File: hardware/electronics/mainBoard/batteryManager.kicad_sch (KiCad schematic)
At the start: 33 parts, among them J20 S3B-XH-SM4-TB, J21 1726480102, Q3 BUK6D72-30EX, Q4 BUK6D72-30EX, U23 BQ76905

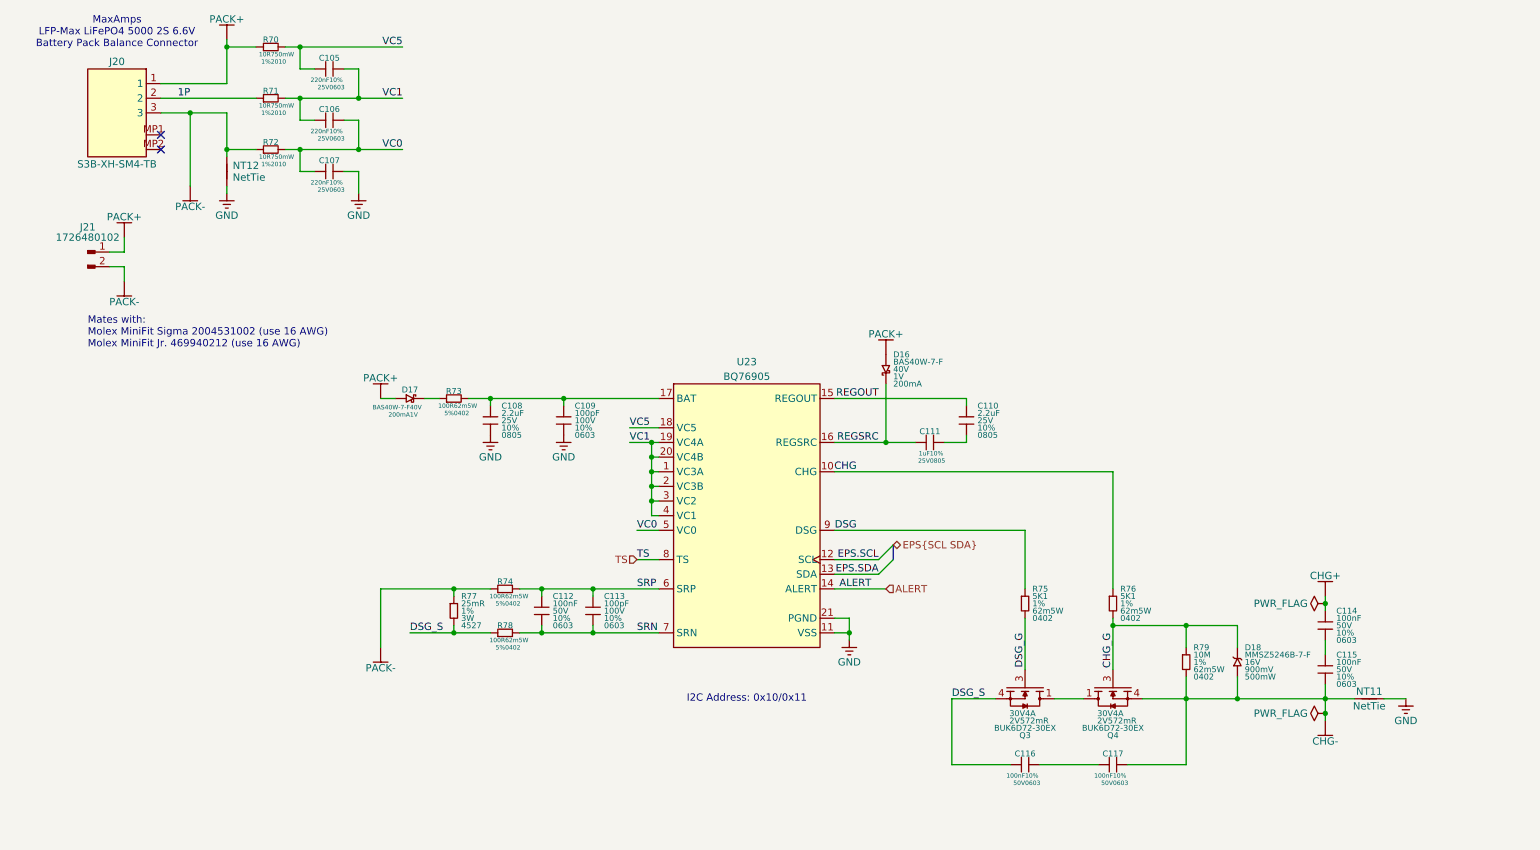
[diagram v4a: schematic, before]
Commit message: updated capacitors
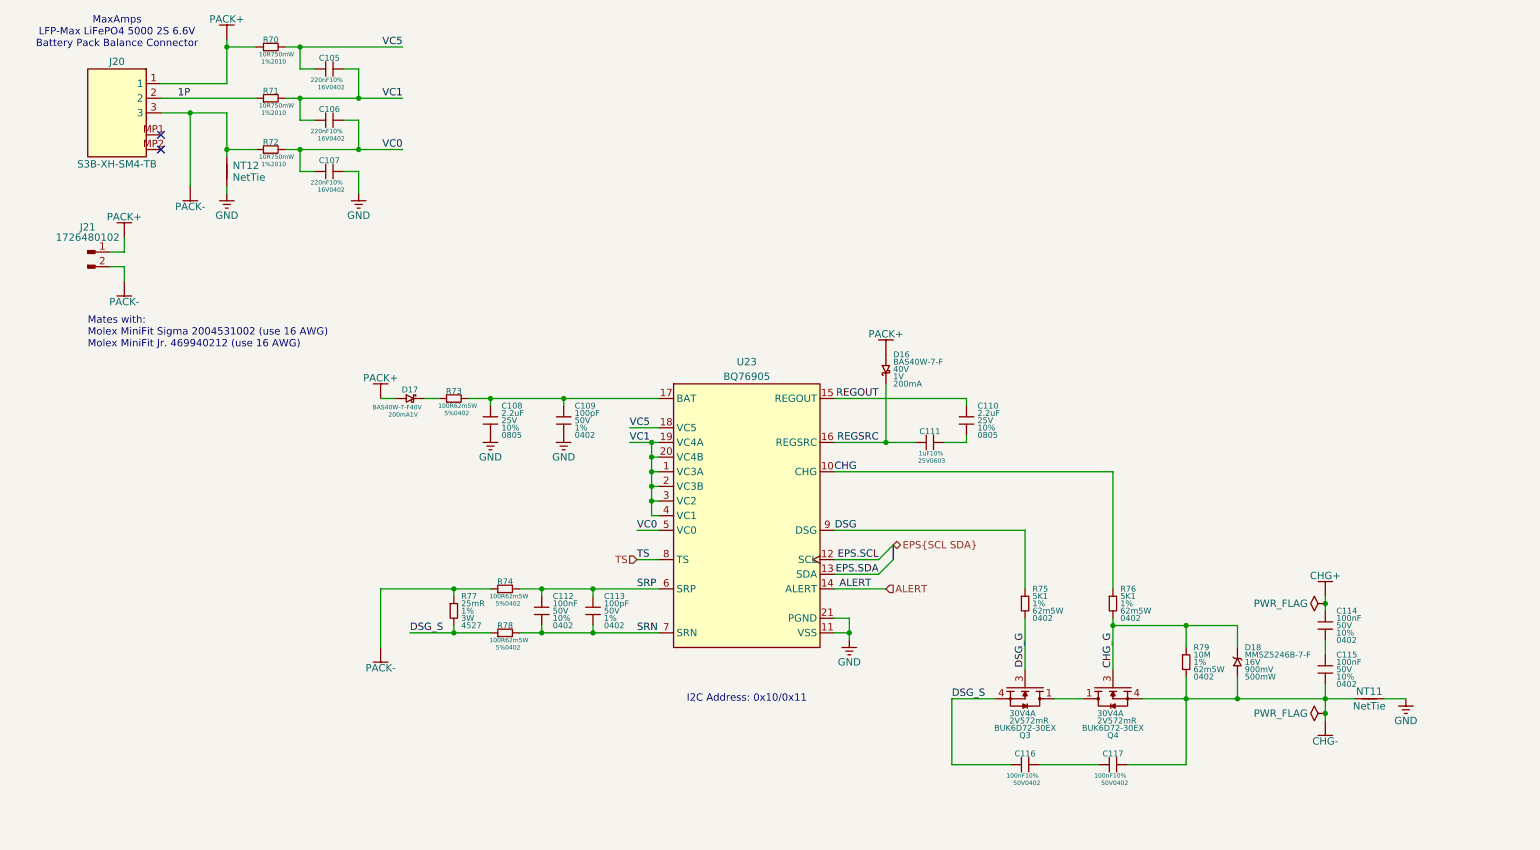
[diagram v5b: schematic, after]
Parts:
- C105, C106, C107: DKPN 478-KAM15BR71E224KTCT-ND -> 490-GRT155R71C224KE01DCT-ND; MPN KAM15BR71E224KT -> GRT155R71C224KE01D; Manufacturer KYOCERA AVX -> Murata Electronics; Package 0603 -> 0402; Voltage Rating 25V -> 16V
- C108, C110: DKPN 478-KAM21KR71E225KUCT-ND -> 490-GRT21BR71E225KE13LCT-ND; MPN 08053C225K4T2A -> GRT21BR71E225KE13L; Manufacturer KYOCERA AVX -> Murata Electronics
- C109, C113: DKPN 478-06031C101K4T2ACT-ND -> 490-14349-1-ND; MPN 06031C101K4T2A -> GCM1555C1H101FA16D; Manufacturer KYOCERA AVX -> Murata Electronics; Package 0603 -> 0402; Tolerance 10% -> 1%; Voltage Rating 100V -> 50V
- C111: DKPN 478-KAF21KR71E105KLCT-ND -> 490-GRT188R71E105KE13DCT-ND; MPN 08053C105K4Z4A -> GRT188R71E105KE13D; Manufacturer KYOCERA AVX -> Murata Electronics; Package 0805 -> 0603
- C112, C114, C115, C116, C117: DKPN 478-KAM15AR71H104KTCT-ND -> 490-GRT155R71H104KE01DCT-ND; MPN 06035C104K4T2A -> GRT155R71H104KE01D; Manufacturer KYOCERA AVX -> Murata Electronics; Package 0603 -> 0402

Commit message: added testpoints and fixed AGND
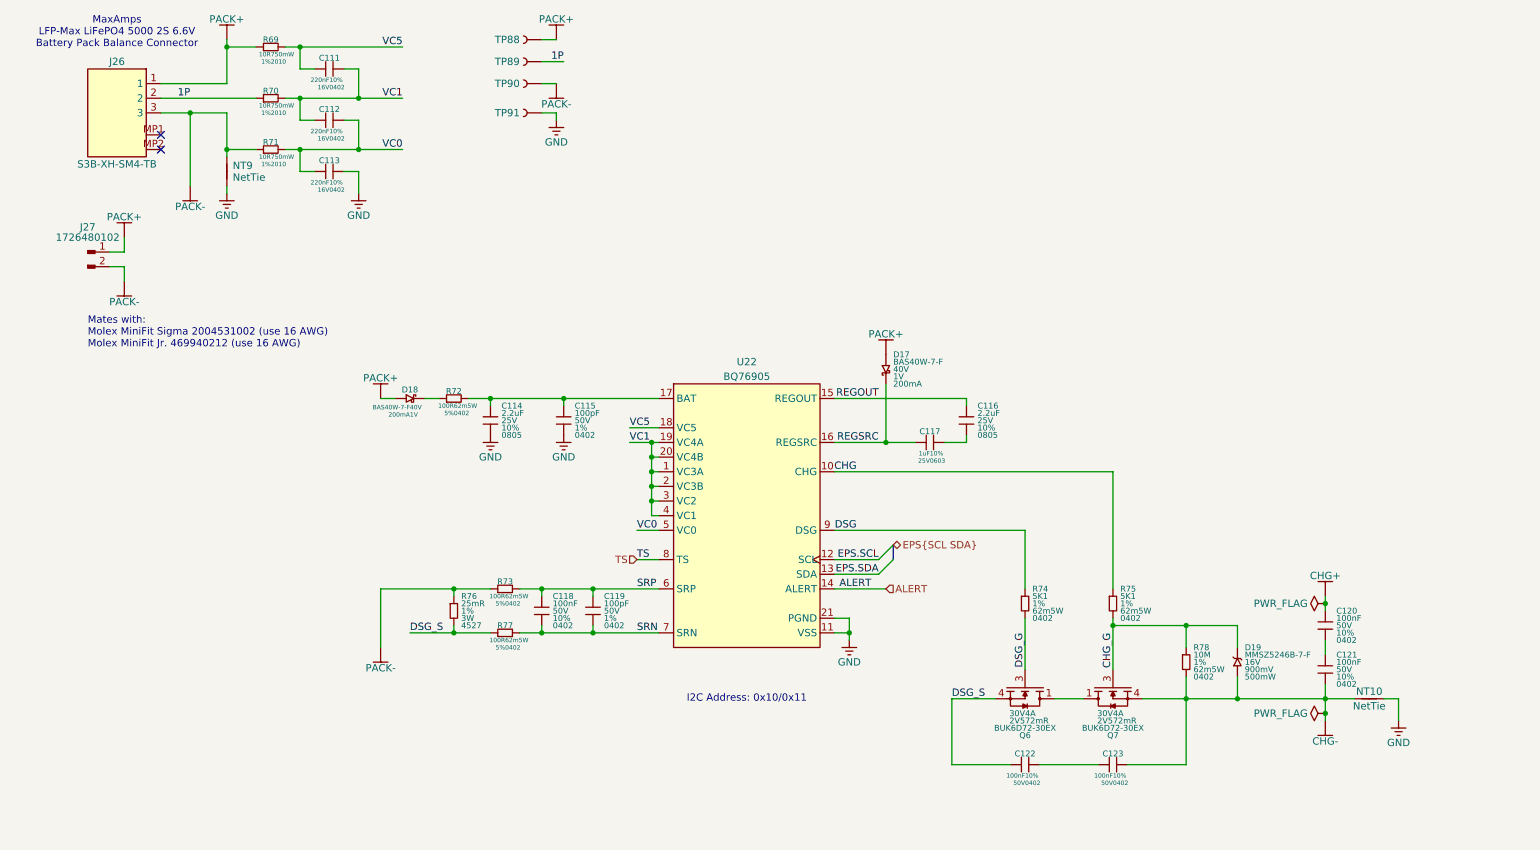
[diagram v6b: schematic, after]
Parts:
- added TP88, TP89: ~, symbol lib_sch:Testpoint
- added TP90, TP91: RCWCTE, symbol lib_sch:Testpoint
- renumbered C105 to C111, C106 to C112, C107 to C113, C108 to C114, C109 to C115, C110 to C116, C111 to C117, C112 to C118, C113 to C119, C114 to C120, C115 to C121, C116 to C122, C117 to C123, D16 to D17, D17 to D18, D18 to D19, J20 to J26, J21 to J27, NT11 to NT10, NT12 to NT9, Q3 to Q6, Q4 to Q7, R70 to R69, R71 to R70, R72 to R71, R73 to R72, R74 to R73, R75 to R74, R76 to R75, R77 to R76, R78 to R77, R79 to R78, U23 to U22
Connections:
- net 1P: now also TP89.1
- net GND: now also TP91.1
- net PACK+: now also TP88.1
- net PACK-: now also TP90.1

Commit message: updated symbol refs
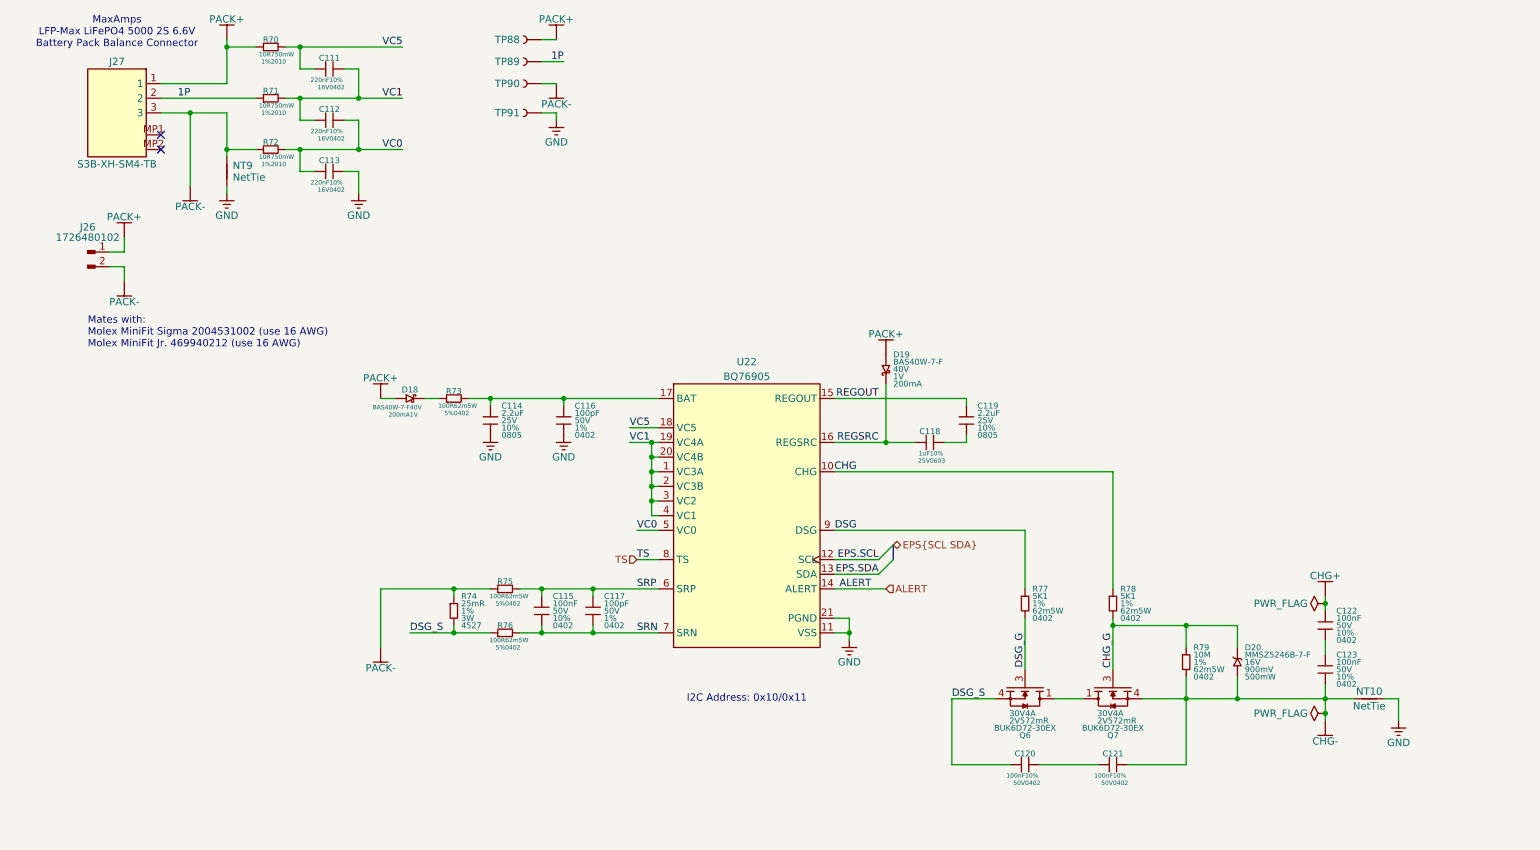
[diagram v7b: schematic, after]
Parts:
- renumbered C118 to C115, C115 to C116, C119 to C117, C117 to C118, C116 to C119, C122 to C120, C123 to C121, C120 to C122, C121 to C123, D17 to D19, D19 to D20, J27 to J26, J26 to J27, R69 to R70, R70 to R71, R71 to R72, R72 to R73, R76 to R74, R73 to R75, R77 to R76, R74 to R77, R75 to R78, R78 to R79

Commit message: updated symbol refs
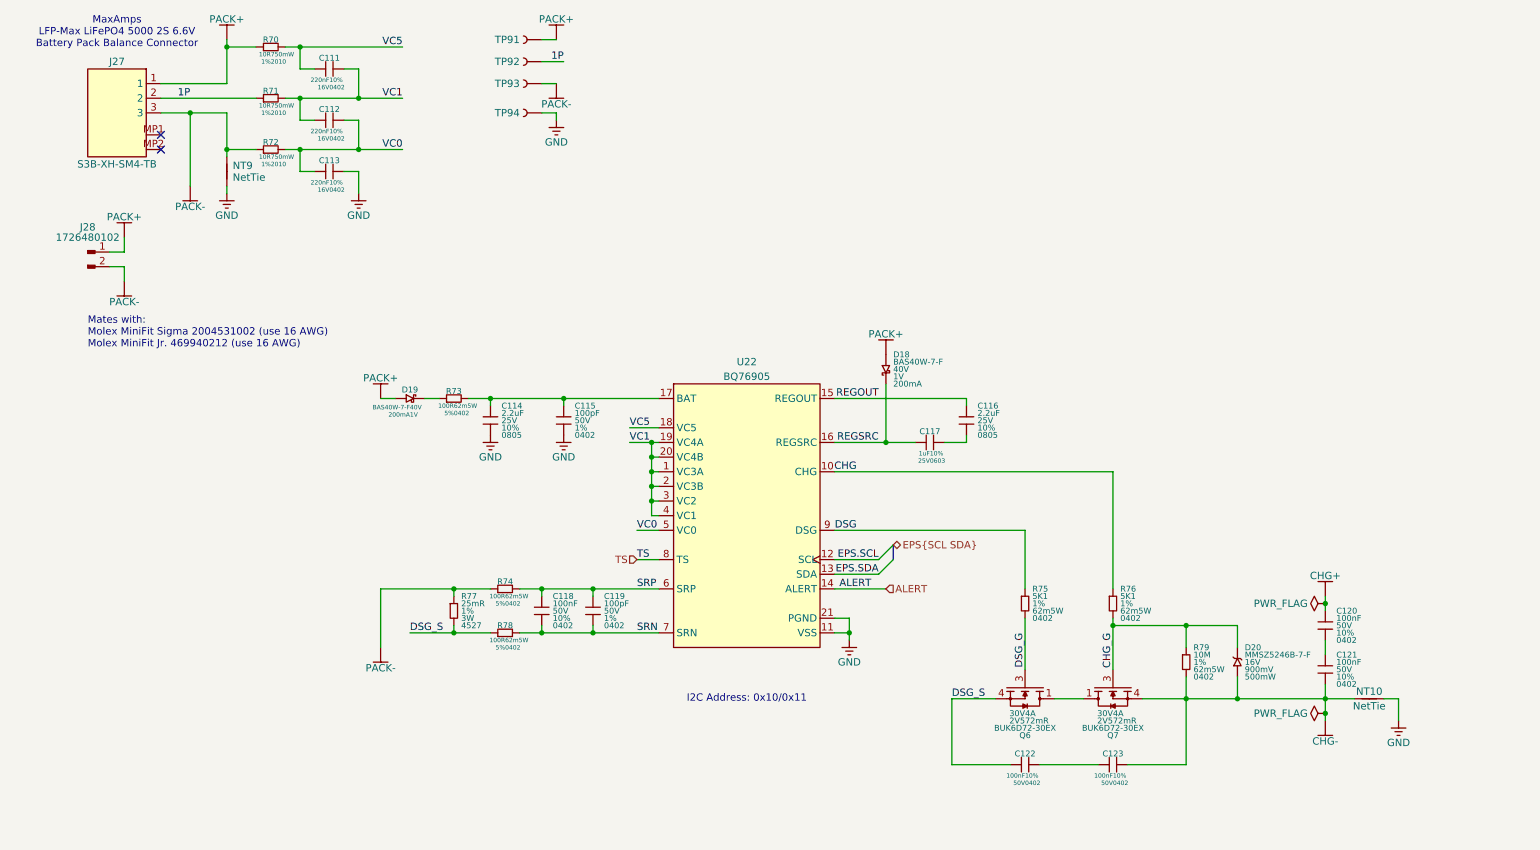
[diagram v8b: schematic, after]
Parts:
- renumbered C116 to C115, C119 to C116, C118 to C117, C115 to C118, C117 to C119, C122 to C120, C123 to C121, C120 to C122, C121 to C123, D19 to D18, D18 to D19, J26 to J28, R75 to R74, R77 to R75, R78 to R76, R74 to R77, R76 to R78, TP88 to TP91, TP89 to TP92, TP90 to TP93, TP91 to TP94
